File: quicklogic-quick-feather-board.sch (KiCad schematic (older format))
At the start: 35 parts, among them IC1 EOS-S3, J5 0473460001, U1 TPS62821DLCR, U2 MCP73831T-2ACI_OT, U3 GD25Q16CWIGR, X1 ECS-_327-12_5-34B-TR

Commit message: Updated internal library
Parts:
- C1: footprint antmicro-footprints:0603-cap -> quicklogic-quick-feather-board-footprints:0603-cap; symbol antmicroCapacitors0603:C_4u7_0603 -> quicklogic-quick-feather-board:C_4u7_0603
- C2, C5: footprint antmicro-footprints:0603-cap -> quicklogic-quick-feather-board-footprints:0603-cap; symbol antmicroCapacitors0603:C_10u_0603 -> quicklogic-quick-feather-board:C_10u_0603
- C3: footprint antmicro-footprints:0402-cap -> quicklogic-quick-feather-board-footprints:0402-cap; symbol antmicroCapacitors0402:C_100p_0402 -> quicklogic-quick-feather-board:C_100p_0402
- C4: footprint antmicro-footprints:0603-cap -> quicklogic-quick-feather-board-footprints:0603-cap; symbol antmicroCapacitors0603:C_22u_0603 -> quicklogic-quick-feather-board:C_22u_0603
- C6, C7: footprint antmicro-footprints:0402-cap -> quicklogic-quick-feather-board-footprints:0402-cap; symbol antmicroCapacitors0402:C_12p_0402 -> quicklogic-quick-feather-board:C_12p_0402
- C8, C9: footprint antmicro-footprints:0402-cap -> quicklogic-quick-feather-board-footprints:0402-cap; symbol antmicroCapacitors0402:C_100n_0402_6V3 -> quicklogic-quick-feather-board:C_100n_0402_6V3
- D1: footprint antmicro-footprints:SOD-123 -> quicklogic-quick-feather-board-footprints:SOD-123; symbol antmicroDiodesRectifiersSingle:MBR0520LT1G -> quicklogic-quick-feather-board:MBR0520LT1G
- D2: footprint antmicro-footprints:LED_0603 -> quicklogic-quick-feather-board-footprints:LED_0603; symbol antmicroLEDIndicationDiscrete:LG_L29K-G2J1-24-Z -> quicklogic-quick-feather-board:LG_L29K-G2J1-24-Z
- D3: footprint antmicro-footprints:SOT-3 -> quicklogic-quick-feather-board-footprints:SOT-3; symbol antmicroTVSDiodes:TPD2EUSB30DRTR -> quicklogic-quick-feather-board:TPD2EUSB30DRTR
- IC1: footprint antmicro-footprints:42-WLCSP -> quicklogic-quick-feather-board-footprints:42-WLCSP; symbol antmicroBGAchips:EOS-S3 -> quicklogic-quick-feather-board:EOS-S3
- J5: footprint antmicro-footprints:USB_Micro_B_Female_0473460001 -> quicklogic-quick-feather-board-footprints:USB_Micro_B_Female_0473460001; symbol antmicroUSBDVIHDMIConnectors:0473460001 -> quicklogic-quick-feather-board:0473460001
- L1: footprint antmicro-footprints:0805-res -> quicklogic-quick-feather-board-footprints:0805-res; symbol antmicroFixedInductors:DFE201610E-R47M=P2 -> quicklogic-quick-feather-board:DFE201610E-R47M=P2
- MIC1: footprint antmicro-footprints:IM69D130 -> quicklogic-quick-feather-board-footprints:IM69D130; symbol antmicroMicrophones:IM69D130 -> quicklogic-quick-feather-board:IM69D130
- R1, R5: footprint antmicro-footprints:0402-res -> quicklogic-quick-feather-board-footprints:0402-res; symbol antmicroResistors0402:R_100k_0402 -> quicklogic-quick-feather-board:R_100k_0402
- R10, R12, R6, R8: footprint antmicro-footprints:0402-res -> quicklogic-quick-feather-board-footprints:0402-res; symbol antmicroResistors0402:R_10k_0402 -> quicklogic-quick-feather-board:R_10k_0402
- R11, R7: footprint antmicro-footprints:0402-res -> quicklogic-quick-feather-board-footprints:0402-res; symbol antmicroResistors0402:R_22R_0402 -> quicklogic-quick-feather-board:R_22R_0402
- R13: footprint antmicro-footprints:0402-res -> quicklogic-quick-feather-board-footprints:0402-res; symbol antmicroResistors0402:R_100R_0402 -> quicklogic-quick-feather-board:R_100R_0402
- R2: footprint antmicro-footprints:0402-res -> quicklogic-quick-feather-board-footprints:0402-res; symbol antmicroResistors0402:R_5k11_0402 -> quicklogic-quick-feather-board:R_5k11_0402
- R3: footprint antmicro-footprints:0402-res -> quicklogic-quick-feather-board-footprints:0402-res; symbol antmicroResistors0402:R_1k_0402 -> quicklogic-quick-feather-board:R_1k_0402
- R4: footprint antmicro-footprints:0402-res -> quicklogic-quick-feather-board-footprints:0402-res; symbol antmicroResistors0402:R_453k_0402 -> quicklogic-quick-feather-board:R_453k_0402
- R9: footprint antmicro-footprints:0402-res -> quicklogic-quick-feather-board-footprints:0402-res; symbol antmicroResistors0402:R_1k5_0402 -> quicklogic-quick-feather-board:R_1k5_0402
- TP1, TP2: footprint antmicro-footprints:Testpoint_smd_1mm -> quicklogic-quick-feather-board-footprints:Testpoint_smd_1mm; symbol antmicroTestPoints:TP_SMD1MM -> quicklogic-quick-feather-board:TP_SMD1MM
- U1: footprint antmicro-footprints:QFN-8_2x1mm -> quicklogic-quick-feather-board-footprints:QFN-8_2x1mm; symbol antmicroDCDCConverters:TPS62821DLCR -> quicklogic-quick-feather-board:TPS62821DLCR
- U2: footprint antmicro-footprints:SOT-753 -> quicklogic-quick-feather-board-footprints:SOT-753; symbol antmicroPMICBatteryChargers:MCP73831T-2ACI_OT -> quicklogic-quick-feather-board:MCP73831T-2ACI_OT
- U3: footprint antmicro-footprints:GD25Q16CWIG -> quicklogic-quick-feather-board-footprints:GD25Q16CWIG; symbol antmicroMemory:GD25Q16CWIGR -> quicklogic-quick-feather-board:GD25Q16CWIGR
- X1: footprint antmicro-footprints:SMD-2_3.2x1.5mm -> quicklogic-quick-feather-board-footprints:SMD-2_3.2x1.5mm; symbol antmicroCrystals:ECS-_327-12_5-34B-TR -> quicklogic-quick-feather-board:ECS-_327-12_5-34B-TR

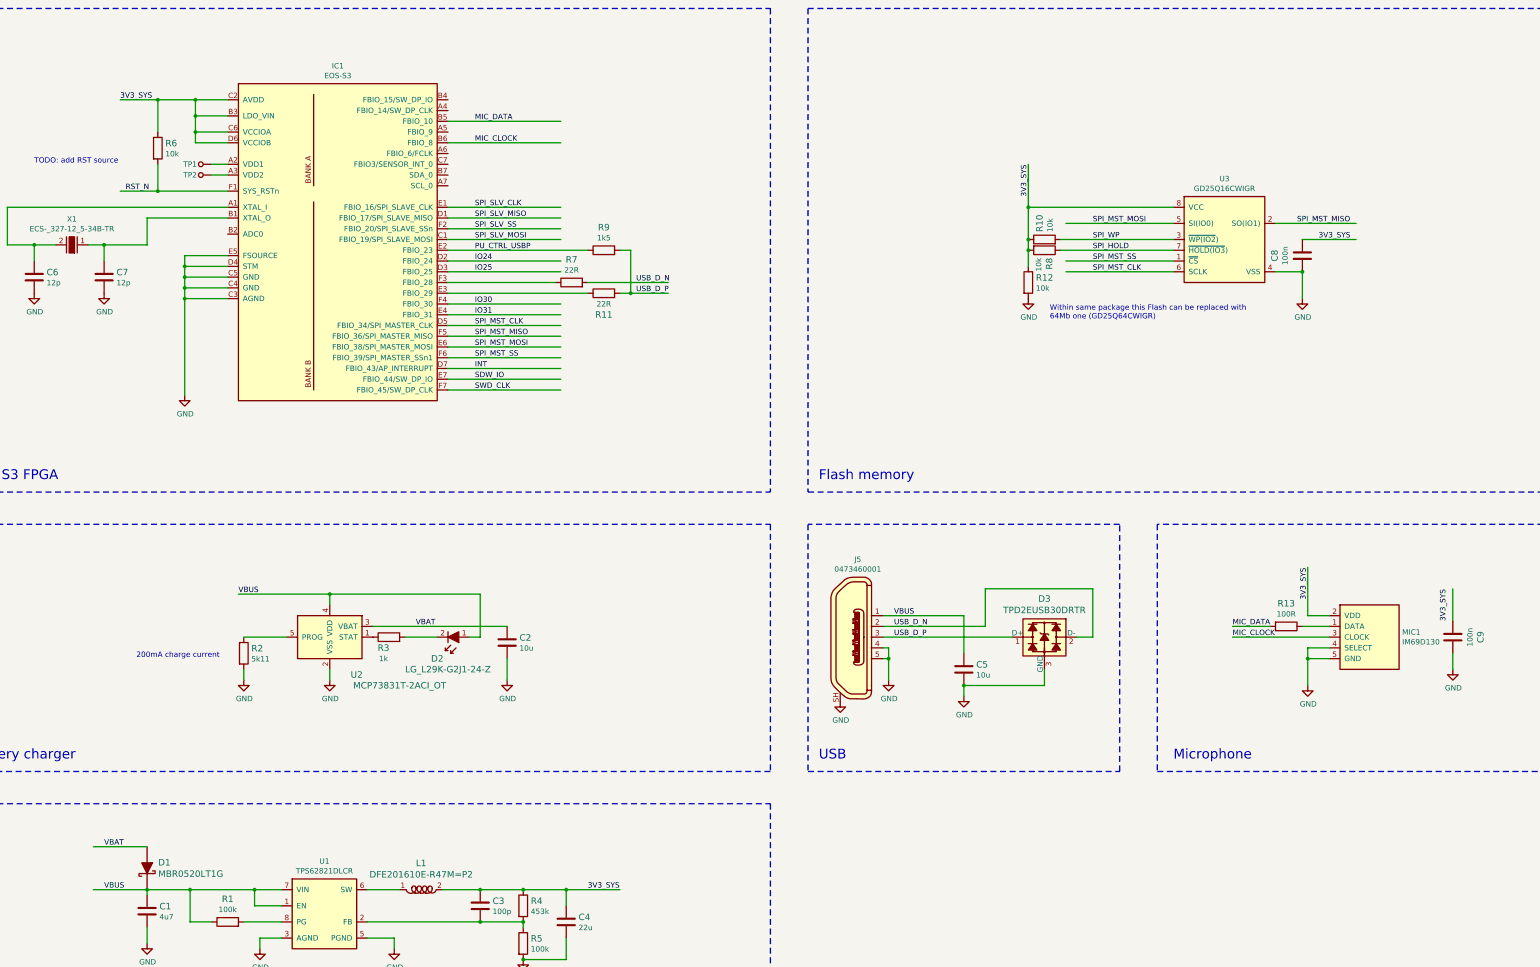
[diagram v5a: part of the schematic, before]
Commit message: Added power rail symbols
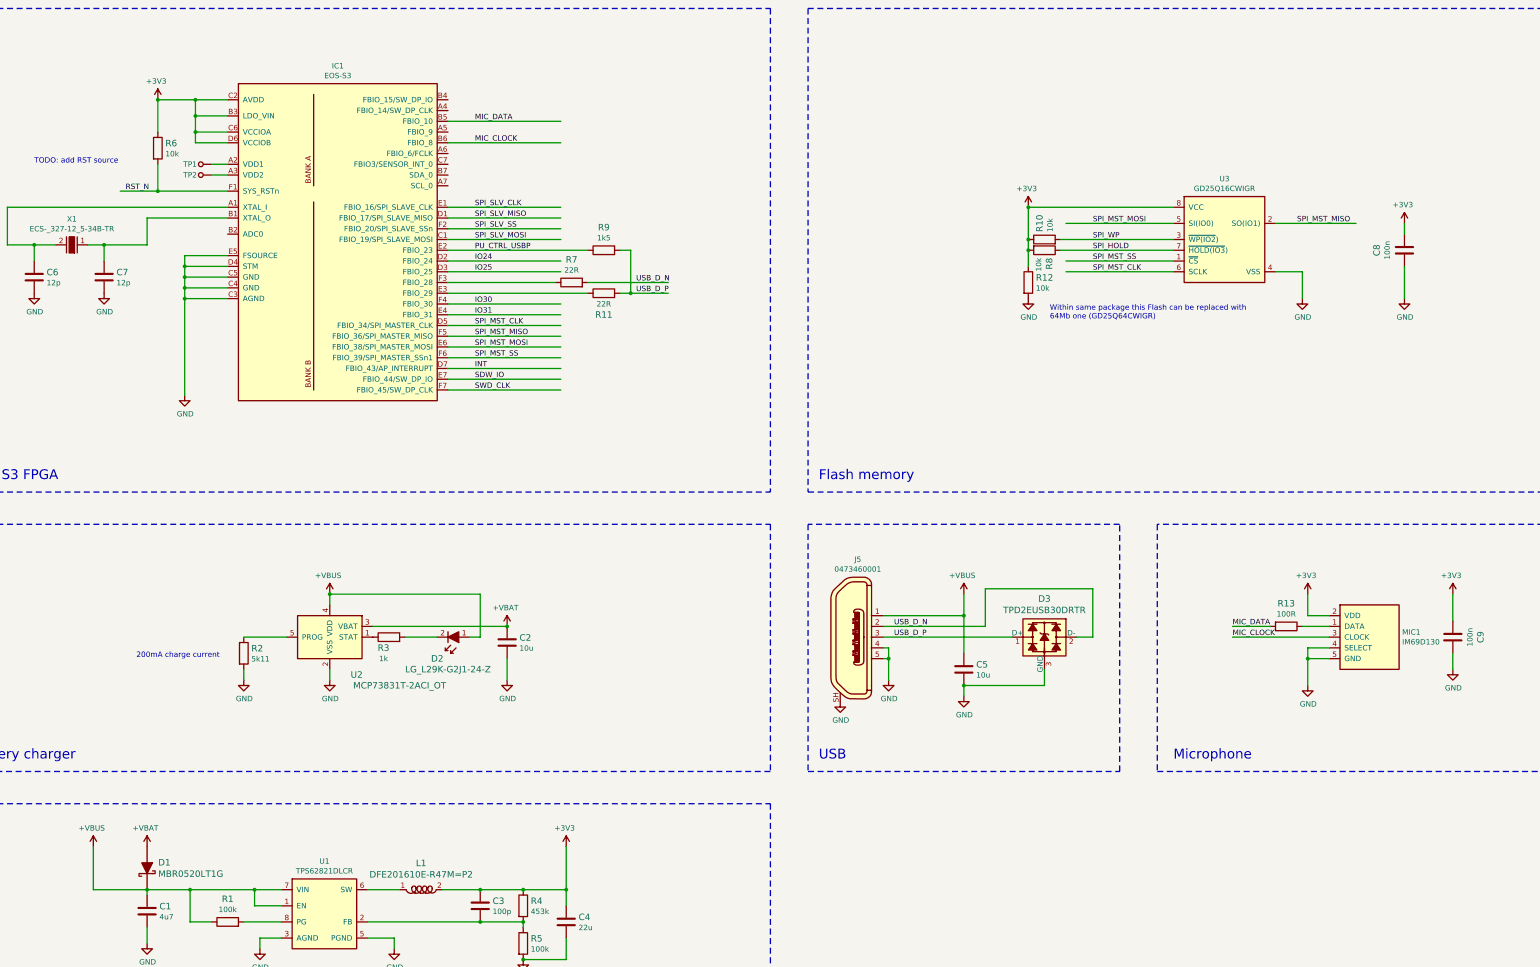
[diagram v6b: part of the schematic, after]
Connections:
- net labels added: +3V3, +VBAT, +VBUS
- net labels removed: 3V3_SYS, VBAT, VBUS
- wire segments 138 -> 137
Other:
- moved on the sheet: C8
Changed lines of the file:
@@
 EESchema Schematic File Version 4
+LIBS:quicklogic-quick-feather-board-cache
 EELAYER 30 0
 EELAYER END
@@
 	1    0    0    -1
 $EndComp
-Text Label 9400 6350 0    50   ~ 0
-VBUS
 Text Label 9400 6550 0    50   ~ 0
 USB_D_P
@@
 	1    0    0    -1
 $EndComp
-Text Label 6550 8900 0    50   ~ 0
-3V3_SYS
 Wire Wire Line
 	3700 8900 3450 8900
-Text Label 2050 8900 0    50   ~ 0
-VBUS
 Wire Wire Line
 	2450 8950 2450 8900
@@
 Text Notes 2350 6750 0    50   ~ 0
 200mA charge current
-Text Label 3300 6150 0    50   ~ 0
-VBUS
 Wire Wire Line
 	4150 6250 4150 6150
-Wire Wire Line
-	4150 6150 3300 6150
-Text Label 4950 6450 0    50   ~ 0
-VBAT
 $Comp
 L quicklogic-quick-feather-board:GND #PWR0108
@@
 	0    1    1    0
 $EndComp
-Wire Wire Line
-	2450 8500 1950 8500
-Text Label 2050 8500 0    50   ~ 0
-VBAT
 $Comp
 L quicklogic-quick-feather-board:TPS62821DLCR U1
@@
 Wire Wire Line
 	12000 2550 10650 2550
-Text Label 10650 2450 1    50   ~ 0
-3V3_SYS
-Wire Wire Line
-	10650 2150 10650 2550
 Wire Wire Line
 	10650 2550 10650 2850
-Connection ~ 10650 2550
 Connection ~ 10650 2850
 Wire Wire Line
@@
 L quicklogic-quick-feather-board:C_100n_0402_6V3 C8
 U 1 1 5DDB4C4D
-P 13200 3000
-F 0 "C8" V 12942 3000 60  0000 C CNN
-F 1 "C_100n_0402_6V3" H 13200 2850 60  0001 C CNN
-F 2 "quicklogic-quick-feather-board-footprints:0402-cap" H 13400 3200 60  0001 L CNN
-F 3 "" H 13200 3000 50  0001 C CNN
-F 4 "Walsin" H 13400 3400 60  0001 L CNN "Manufacturer"
-F 5 "0402X104K6R3CT" H 13400 3300 60  0001 L CNN "MPN"
-F 6 "100n" V 13040 3000 50  0000 C CNN "Val"
-	1    13200 3000
+P 14150 2950
+F 0 "C8" V 13892 2950 60  0000 C CNN
+F 1 "C_100n_0402_6V3" H 14150 2800 60  0001 C CNN
+F 2 "quicklogic-quick-feather-board-footprints:0402-cap" H 14350 3150 60  0001 L CNN
+F 3 "" H 14150 2950 50  0001 C CNN
+F 4 "Walsin" H 14350 3350 60  0001 L CNN "Manufacturer"
+F 5 "0402X104K6R3CT" H 14350 3250 60  0001 L CNN "MPN"
+F 6 "100n" V 13990 2950 50  0000 C CNN "Val"
+	1    14150 2950
 	1    0    0    -1
 $EndComp
@@
 	1    0    0    -1
 $EndComp
-Wire Wire Line
-	12950 3150 13200 3150
-Wire Wire Line
-	13200 3150 13200 3400
 $Comp
 L quicklogic-quick-feather-board:R_10k_0402 R12
@@
 	0    1    1    0
 $EndComp
-Connection ~ 13200 3150
-Wire Wire Line
-	13200 2850 13700 2850
-Text Label 13350 2850 0    50   ~ 0
-3V3_SYS
 Text Label 11250 2850 0    50   ~ 0
 SPI_WP
@@
 Wire Wire Line
 	6350 9050 6350 8900
-Connection ~ 6350 8900
-Wire Wire Line
-	6350 8900 6850 8900
 Text Label 7000 3250 0    50   ~ 0
 USB_D_N
@@
 Wire Notes Line
 	11500 5500 8600 5500
-Text Label 2200 1550 0    50   ~ 0
-3V3_SYS
 Connection ~ 2550 2400
-Wire Wire Line
-	2200 1550 2550 1550
 Wire Wire Line
 	2550 2150 2550 2400
@@
 Wire Wire Line
 	13450 6350 13250 6350
-Wire Wire Line
-	13250 6350 13250 5900
 Wire Wire Line
 	13450 6750 13250 6750
@@
 	13250 6650 13250 6750
 Connection ~ 13250 6750
-Text Label 13250 6200 1    50   ~ 0
-3V3_SYS
 Text Label 12550 6450 0    50   ~ 0
 MIC_DATA
@@
 	-1   0    0    1
 $EndComp
-Text Label 14550 6400 1    50   ~ 0
-3V3_SYS
-Wire Wire Line
-	14600 6100 14600 6400
 Wire Wire Line
 	14600 6700 14600 6850
@@
 	10800 7000 10050 7000
 Connection ~ 10050 7000
+$Comp
+L quicklogic-quick-feather-board:+3V3 #PWR0112
+U 1 1 5DE2E29D
+P 2550 1500
+F 0 "#PWR0112" H 2550 1500 50  0001 C CNN
+F 1 "+3V3" H 2535 1623 50  0000 C CNN
+F 2 "" H 2550 1500 50  0001 C CNN
+F 3 "" H 2550 1500 50  0001 C CNN
+	1    2550 1500
+	1    0    0    -1
+$EndComp
+$Comp
+L quicklogic-quick-feather-board:+3V3 #PWR0113
+U 1 1 5DE33E97
+P 10650 2500
+F 0 "#PWR0113" H 10650 2500 50  0001 C CNN
+F 1 "+3V3" H 10635 2623 50  0000 C CNN
+F 2 "" H 10650 2500 50  0001 C CNN
+F 3 "" H 10650 2500 50  0001 C CNN
+	1    10650 2500
+	1    0    0    -1
+$EndComp
+Connection ~ 10650 2550
+$Comp
+L quicklogic-quick-feather-board:+3V3 #PWR0114
+U 1 1 5DE34948
+P 14150 2650
+F 0 "#PWR0114" H 14150 2650 50  0001 C CNN
+F 1 "+3V3" H 14135 2773 50  0000 C CNN
+F 2 "" H 14150 2650 50  0001 C CNN
+F 3 "" H 14150 2650 50  0001 C CNN
+	1    14150 2650
+	1    0    0    -1
+$EndComp
+Wire Wire Line
+	12950 3150 13200 3150
+Wire Wire Line
+	13200 3150 13200 3400
+Wire Wire Line
+	14150 3100 14150 3400
+$Comp
+L quicklogic-quick-feather-board:GND #PWR0115
+U 1 1 5DE3FA98
+P 14150 3400
+F 0 "#PWR0115" H 14150 3150 50  0001 C CNN
+F 1 "GND" H 14155 3227 50  0000 C CNN
+F 2 "" H 14150 3400 50  0001 C CNN
+F 3 "" H 14150 3400 50  0001 C CNN
+	1    14150 3400
+	1    0    0    -1
+$EndComp
+Wire Wire Line
+	14150 2700 14150 2800
+$Comp
+L quicklogic-quick-feather-board:+3V3 #PWR0116
+U 1 1 5DE4A7B8
+P 14600 6100
+F 0 "#PWR0116" H 14600 6100 50  0001 C CNN
+F 1 "+3V3" H 14585 6223 50  0000 C CNN
+F 2 "" H 14600 6100 50  0001 C CNN
+F 3 "" H 14600 6100 50  0001 C CNN
+	1    14600 6100
+	1    0    0    -1
+$EndComp
+$Comp
+L quicklogic-quick-feather-board:+3V3 #PWR0117
+U 1 1 5DE50B3C
+P 13250 6100
+F 0 "#PWR0117" H 13250 6100 50  0001 C CNN
+F 1 "+3V3" H 13235 6223 50  0000 C CNN
+F 2 "" H 13250 6100 50  0001 C CNN
+F 3 "" H 13250 6100 50  0001 C CNN
+	1    13250 6100
+	1    0    0    -1
+$EndComp
+Wire Wire Line
+	13250 6150 13250 6350
+Wire Wire Line
+	14600 6150 14600 6400
+$Comp
+L quicklogic-quick-feather-board:+3V3 #PWR0118
+U 1 1 5DE5BFA1
+P 6350 8450
+F 0 "#PWR0118" H 6350 8450 50  0001 C CNN
+F 1 "+3V3" H 6335 8573 50  0000 C CNN
+F 2 "" H 6350 8450 50  0001 C CNN
+F 3 "" H 6350 8450 50  0001 C CNN
+	1    6350 8450
+	1    0    0    -1
+$EndComp
+Connection ~ 6350 8900
+$Comp
+L quicklogic-quick-feather-board:+VBUS #PWR0119
+U 1 1 5DE69BB0
+P 4150 6100
+F 0 "#PWR0119" H 4150 6100 50  0001 C CNN
+F 1 "+VBUS" H 4135 6223 50  0000 C CNN
+F 2 "" H 4150 6100 50  0001 C CNN
+F 3 "" H 4150 6100 50  0001 C CNN
+	1    4150 6100
+	1    0    0    -1
+$EndComp
+$Comp
+L quicklogic-quick-feather-board:+VBAT #PWR0120
+U 1 1 5DE6A679
+P 5800 6400
+F 0 "#PWR0120" H 5800 6400 50  0001 C CNN
+F 1 "+VBAT" H 5785 6523 50  0000 C CNN
+F 2 "" H 5800 6400 50  0001 C CNN
+F 3 "" H 5800 6400 50  0001 C CNN
+	1    5800 6400
+	1    0    0    -1
+$EndComp
+Connection ~ 5800 6450
+$Comp
+L quicklogic-quick-feather-board:+VBAT #PWR0121
+U 1 1 5DE6ABAC
+P 2450 8450
+F 0 "#PWR0121" H 2450 8450 50  0001 C CNN
+F 1 "+VBAT" H 2435 8573 50  0000 C CNN
+F 2 "" H 2450 8450 50  0001 C CNN
+F 3 "" H 2450 8450 50  0001 C CNN
+	1    2450 8450
+	1    0    0    -1
+$EndComp
+$Comp
+L quicklogic-quick-feather-board:+VBUS #PWR0122
+U 1 1 5DE6B20E
+P 1950 8450
+F 0 "#PWR0122" H 1950 8450 50  0001 C CNN
+F 1 "+VBUS" H 1935 8573 50  0000 C CNN
+F 2 "" H 1950 8450 50  0001 C CNN
+F 3 "" H 1950 8450 50  0001 C CNN
+	1    1950 8450
+	1    0    0    -1
+$EndComp
+Wire Wire Line
+	1950 8900 1950 8500
+Wire Wire Line
+	6350 8500 6350 8900
+$Comp
+L quicklogic-quick-feather-board:+VBUS #PWR0123
+U 1 1 5DE7906C
+P 10050 6100
+F 0 "#PWR0123" H 10050 6100 50  0001 C CNN
+F 1 "+VBUS" H 10035 6223 50  0000 C CNN
+F 2 "" H 10050 6100 50  0001 C CNN
+F 3 "" H 10050 6100 50  0001 C CNN
+	1    10050 6100
+	1    0    0    -1
+$EndComp
+Wire Wire Line
+	10050 6150 10050 6350
+Connection ~ 10050 6350
 $EndSCHEMATC
